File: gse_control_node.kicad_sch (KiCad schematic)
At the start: 9 parts

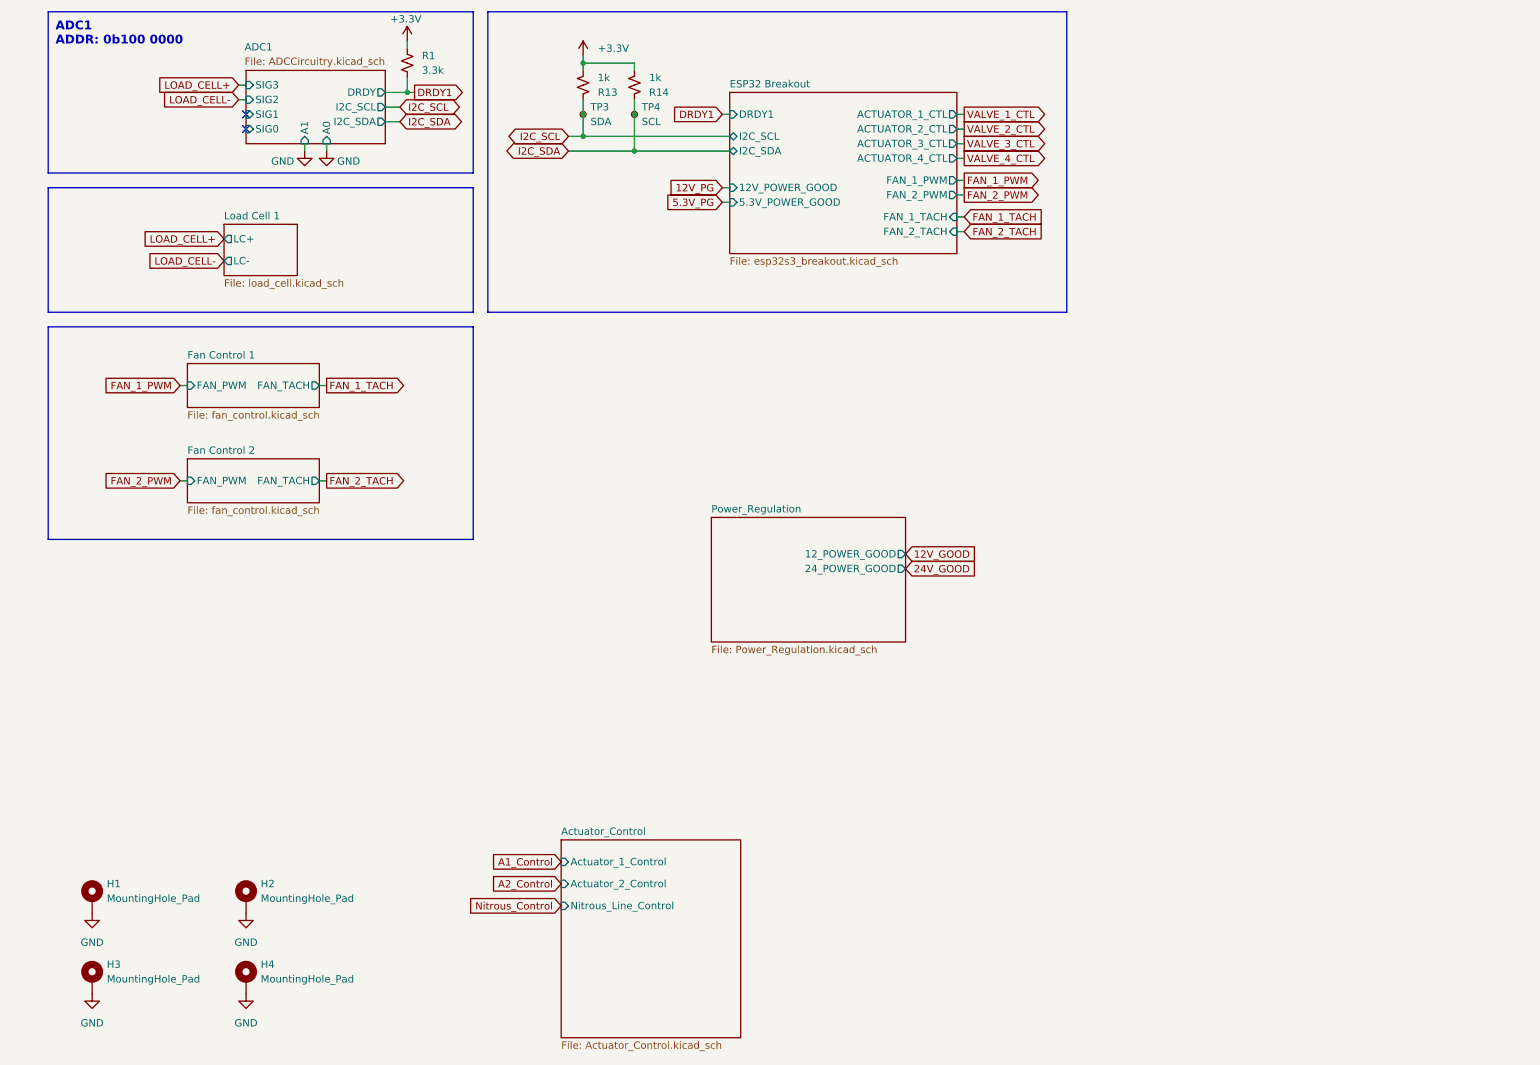
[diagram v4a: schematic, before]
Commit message: update buck converter components and add reverse polarity protection
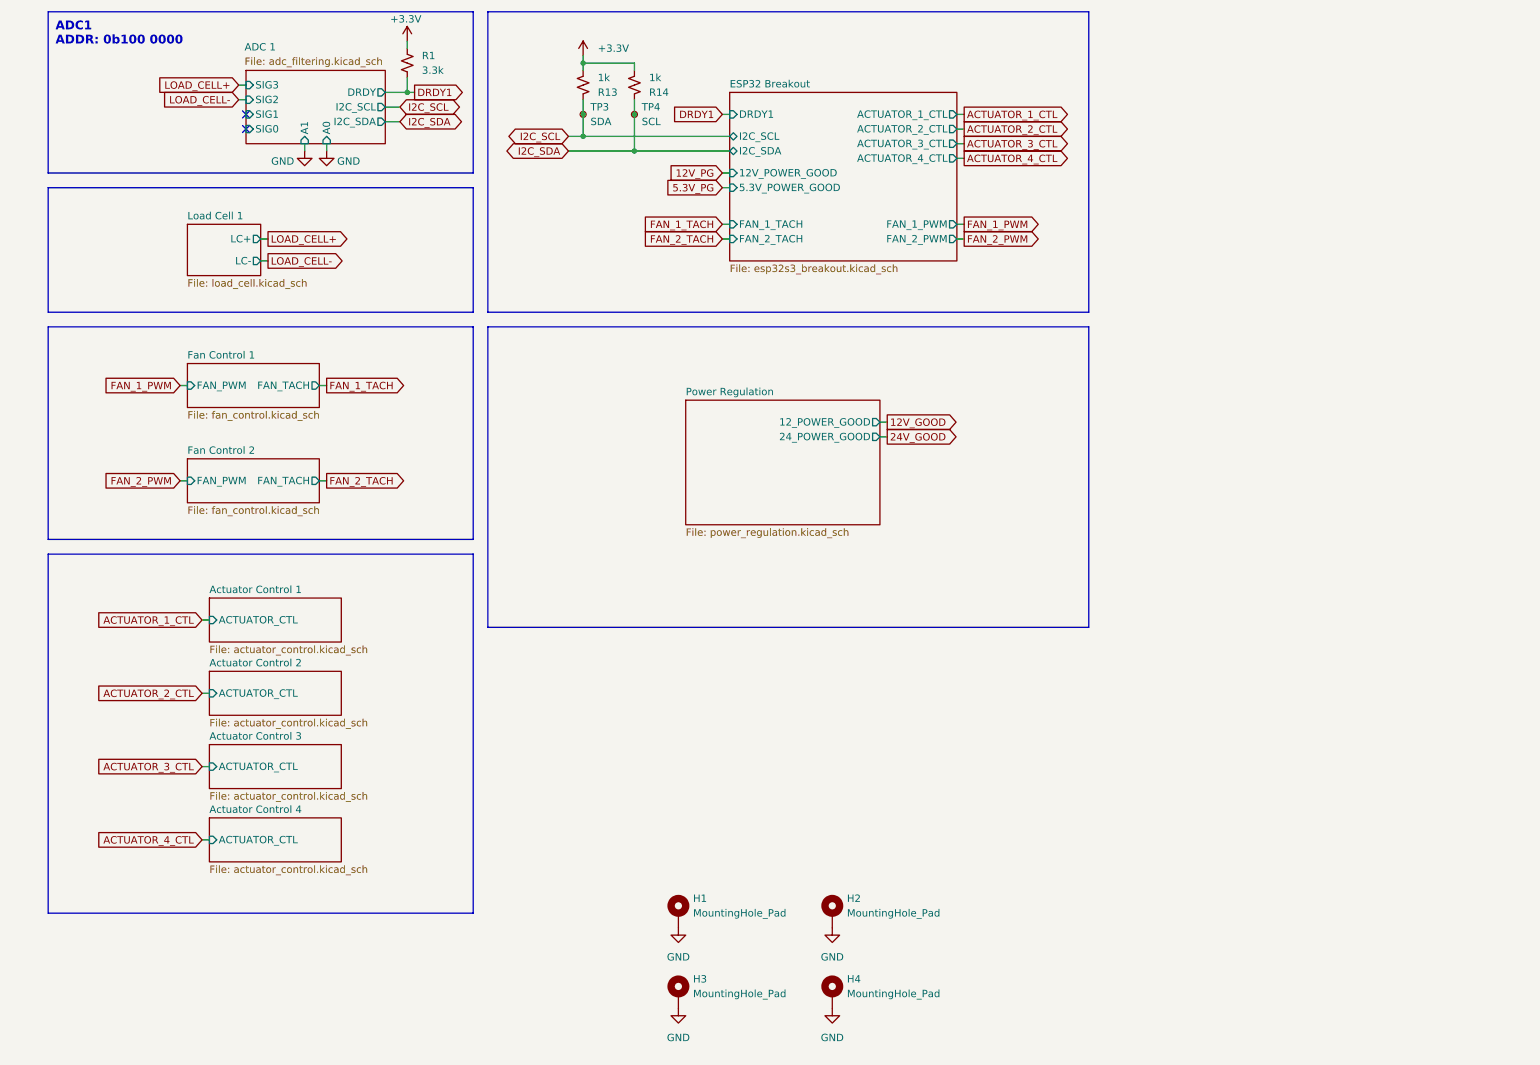
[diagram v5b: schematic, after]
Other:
- sheet ADC1 renamed ADC 1
- sheet Power_Regulation renamed Power Regulation
- removed sheet Actuator_Control
- added sheet Actuator Control 1 (actuator_control.kicad_sch)
- added sheet Actuator Control 2 (actuator_control.kicad_sch)
- added sheet Actuator Control 3 (actuator_control.kicad_sch)
- added sheet Actuator Control 4 (actuator_control.kicad_sch)
- sheet ADC 1: file ADCCircuitry.kicad_sch -> adc_filtering.kicad_sch
- sheet Power Regulation: file Power_Regulation.kicad_sch -> power_regulation.kicad_sch
- moved on the sheet: H1, H2, H3, H4

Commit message: do some pcb routing
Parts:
- added J1: Screw_Terminal_01x02, TerminalBlock_Phoenix:TerminalBlock_Phoenix_MKDS-1,5-2_1x02_P5.00mm_Horizontal, symbol Connector:Screw_Terminal_01x02
- renumbered H3 to H2, H2 to H3, R13 to R2, R14 to R3, TP3 to TP1, TP4 to TP2
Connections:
- net ADC 1/SIG0: now also J1.1 (Pin_1)
- net ADC 1/SIG1: now also J1.2 (Pin_2)
- no-connect marks 2 -> 0
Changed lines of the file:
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@@
 		(color 0 0 0 0)
 	)
-	(no_connect
-		(at 49.53 33.02)
-	)
-	(no_connect
-		(at 49.53 35.56)
-	)
 	(wire
 		(pts
@@
 	(wire
 		(pts
+			(xy 33.02 35.56) (xy 49.53 35.56)
+		)
+		(stroke
+			(width 0)
+			(type default)
+		)
+	)
+	(wire
+		(pts
 			(xy 38.1 96.52) (xy 39.37 96.52)
 		)
@@
 		(pts
 			(xy 73.66 29.21) (xy 77.47 29.21)
+		)
+		(stroke
+			(width 0)
+			(type default)
+		)
+	)
+	(wire
+		(pts
+			(xy 33.02 33.02) (xy 49.53 33.02)
 		)
 		(stroke
@@
 		(in_pos_files yes)
 		(dnp no)
-		(property "Reference" "#PWR07"
+		(property "Reference" "#PWR01"
 			(at 59.69 45.72 0)
 			(hide yes)
@@
 			(project "gse_control_node"
 				(path "/24817451-dfe0-4b9a-9d93-7304529c9d58"
-					(reference "#PWR07")
+					(reference "#PWR01")
 					(unit 1)
 				)
@@
 		(dnp no)
 		(fields_autoplaced yes)
-		(property "Reference" "#PWR03"
+		(property "Reference" "#PWR05"
 			(at 124.46 180.34 0)
 			(hide yes)
@@
 			(project "gse_control_node"
 				(path "/24817451-dfe0-4b9a-9d93-7304529c9d58"
-					(reference "#PWR03")
+					(reference "#PWR05")
 					(unit 1)
 				)
@@
 		(in_pos_files yes)
 		(dnp no)
-		(property "Reference" "#PWR013"
+		(property "Reference" "#PWR03"
 			(at 77.47 24.13 0)
 			(hide yes)
@@
 			(project "gse_control_node"
 				(path "/24817451-dfe0-4b9a-9d93-7304529c9d58"
-					(reference "#PWR013")
+					(reference "#PWR03")
 					(unit 1)
 				)
@@
 		(dnp no)
 		(fields_autoplaced yes)
-		(property "Reference" "#PWR06"
+		(property "Reference" "#PWR08"
 			(at 151.13 194.31 0)
 			(hide yes)
@@
 			(project "gse_control_node"
 				(path "/24817451-dfe0-4b9a-9d93-7304529c9d58"
-					(reference "#PWR06")
+					(reference "#PWR08")
 					(unit 1)
 				)
@@
 		(dnp no)
 		(fields_autoplaced yes)
-		(property "Reference" "R13"
+		(property "Reference" "R2"
 			(at 110.49 29.2101 0)
 			(show_name no)
@@
 			(project "gse_control_node"
 				(path "/24817451-dfe0-4b9a-9d93-7304529c9d58"
-					(reference "R13")
+					(reference "R2")
 					(unit 1)
 				)
@@
 		(in_pos_files yes)
 		(dnp no)
-		(property "Reference" "#PWR09"
+		(property "Reference" "#PWR02"
 			(at 63.5 45.72 0)
 			(hide yes)
@@
 			(project "gse_control_node"
 				(path "/24817451-dfe0-4b9a-9d93-7304529c9d58"
-					(reference "#PWR09")
+					(reference "#PWR02")
 					(unit 1)
 				)
@@
 		(dnp no)
 		(fields_autoplaced yes)
-		(property "Reference" "R14"
+		(property "Reference" "R3"
 			(at 119.38 29.2101 0)
 			(show_name no)
@@
 			(project "gse_control_node"
 				(path "/24817451-dfe0-4b9a-9d93-7304529c9d58"
-					(reference "R14")
+					(reference "R3")
 					(unit 1)
 				)
@@
 		(dnp no)
 		(fields_autoplaced yes)
-		(property "Reference" "#PWR020"
+		(property "Reference" "#PWR04"
 			(at 107.95 26.67 0)
 			(hide yes)
@@
 			(project "gse_control_node"
 				(path "/24817451-dfe0-4b9a-9d93-7304529c9d58"
-					(reference "#PWR020")
+					(reference "#PWR04")
 					(unit 1)
 				)
@@
 		(dnp no)
 		(fields_autoplaced yes)
-		(property "Reference" "#PWR05"
+		(property "Reference" "#PWR06"
 			(at 124.46 194.31 0)
 			(hide yes)
@@
 			(project "gse_control_node"
 				(path "/24817451-dfe0-4b9a-9d93-7304529c9d58"
-					(reference "#PWR05")
+					(reference "#PWR06")
 					(unit 1)
 				)
@@
 		(dnp no)
 		(fields_autoplaced yes)
-		(property "Reference" "#PWR04"
+		(property "Reference" "#PWR07"
 			(at 151.13 180.34 0)
 			(hide yes)
@@
 			(project "gse_control_node"
 				(path "/24817451-dfe0-4b9a-9d93-7304529c9d58"
-					(reference "#PWR04")
+					(reference "#PWR07")
+					(unit 1)
+				)
+			)
+		)
+	)
+	(symbol
+		(lib_id "Connector:Screw_Terminal_01x02")
+		(at 27.94 35.56 180)
+		(unit 1)
+		(body_style 1)
+		(exclude_from_sim no)
+		(in_bom yes)
+		(on_board yes)
+		(in_pos_files yes)
+		(dnp no)
+		(property "Reference" "J1"
+			(at 27.94 30.226 0)
+			(show_name no)
+			(do_not_autoplace no)
+			(effects
+				(font
+					(size 1.27 1.27)
+				)
+			)
+		)
+		(property "Value" "Screw_Terminal_01x02"
+			(at 27.94 29.21 0)
+			(hide yes)
+			(show_name no)
+			(do_not_autoplace no)
+			(effects
+				(font
+					(size 1.27 1.27)
+				)
+			)
+		)
+		(property "Footprint" "TerminalBlock_Phoenix:TerminalBlock_Phoenix_MKDS-1,5-2_1x02_P5.00mm_Horizontal"
+			(at 27.94 35.56 0)
+			(hide yes)
+			(show_name no)
+			(do_not_autoplace no)
+			(effects
+				(font
+					(size 1.27 1.27)
+				)
+			)
+		)
+		(property "Datasheet" ""
+			(at 27.94 35.56 0)
+			(hide yes)
+			(show_name no)
+			(do_not_autoplace no)
+			(effects
+				(font
+					(size 1.27 1.27)
+				)
+			)
+		)
+		(property "Description" "Generic screw terminal, single row, 01x02, script generated (kicad-library-utils/schlib/autogen/connector/)"
+			(at 27.94 35.56 0)
+			(hide yes)
+			(show_name no)
+			(do_not_autoplace no)
+			(effects
+				(font
+					(size 1.27 1.27)
+				)
+			)
+		)
+		(pin "1"
+		)
+		(pin "2"
+		)
+		(instances
+			(project "gse_control_node"
+				(path "/24817451-dfe0-4b9a-9d93-7304529c9d58"
+					(reference "J1")
 					(unit 1)
 				)
@@
 		(dnp no)
 		(fields_autoplaced yes)
-		(property "Reference" "TP3"
+		(property "Reference" "TP1"
 			(at 109.22 31.7499 0)
 			(show_name no)
@@
 			(project "gse_control_node"
 				(path "/24817451-dfe0-4b9a-9d93-7304529c9d58"
-					(reference "TP3")
+					(reference "TP1")
 					(unit 1)
 				)
@@
 		(dnp no)
 		(fields_autoplaced yes)
-		(property "Reference" "H2"
+		(property "Reference" "H3"
 			(at 153.67 168.9099 0)
 			(show_name no)
@@
 			(project "gse_control_node"
 				(path "/24817451-dfe0-4b9a-9d93-7304529c9d58"
-					(reference "H2")
+					(reference "H3")
 					(unit 1)
 				)
@@
 		(dnp no)
 		(fields_autoplaced yes)
-		(property "Reference" "TP4"
+		(property "Reference" "TP2"
 			(at 118.11 31.7499 0)
 			(show_name no)
@@
 			(project "gse_control_node"
 				(path "/24817451-dfe0-4b9a-9d93-7304529c9d58"
-					(reference "TP4")
+					(reference "TP2")
 					(unit 1)
 				)
@@
 		(dnp no)
 		(fields_autoplaced yes)
-		(property "Reference" "H3"
+		(property "Reference" "H2"
 			(at 127 182.8799 0)
 			(show_name no)
@@
 			(project "gse_control_node"
 				(path "/24817451-dfe0-4b9a-9d93-7304529c9d58"
-					(reference "H3")
+					(reference "H2")
 					(unit 1)
 				)

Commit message: finish pcb routing
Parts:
- removed TP1: SDA, TestPoint:TestPoint_Pad_D1.5mm, symbol Connector:TestPoint_Small
- removed TP2: SCL, TestPoint:TestPoint_Pad_D1.5mm, symbol Connector:TestPoint_Small
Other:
- sheet ESP32 Breakout ports: added 5.17V_POWER_GOOD; removed 5.3V_POWER_GOOD
- sheet Power Regulation ports: added 5.17_POWER_GOOD; removed 24_POWER_GOOD

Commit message: remove unneccesary component fields
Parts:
- H1, H2, H3, H4: LCSC (none) -> N/A
- J1: LCSC (none) -> N/A; now left out of the parts list
- R1: value 3.3k -> 3.3kΩ; LCSC C25890 -> (none); MPN 0402WGF3301TCE -> (none)
- R2, R3: value 1k -> 1kΩ; LCSC C11702 -> (none)
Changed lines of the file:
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@@
 		(in_bom no)
 		(on_board yes)
-		(in_pos_files yes)
+		(in_pos_files no)
 		(dnp no)
 		(fields_autoplaced yes)
@@
 			)
 		)
+		(property "LCSC" "N/A"
+			(at 151.13 185.42 0)
+			(hide yes)
+			(show_name no)
+			(do_not_autoplace no)
+			(effects
+				(font
+					(size 1.27 1.27)
+				)
+			)
+		)
 		(pin "1"
 		)
@@
 		(in_bom no)
 		(on_board yes)
-		(in_pos_files yes)
+		(in_pos_files no)
 		(dnp no)
 		(fields_autoplaced yes)
@@
 			)
 		)
+		(property "LCSC" "N/A"
+			(at 124.46 171.45 0)
+			(hide yes)
+			(show_name no)
+			(do_not_autoplace no)
+			(effects
+				(font
+					(size 1.27 1.27)
+				)
+			)
+		)
 		(pin "1"
 		)
@@
 			)
 		)
-		(property "Value" "1k"
+		(property "Value" "1kΩ"
 			(at 110.49 26.6701 0)
 			(show_name no)
@@
 			)
 		)
-		(property "ADC Number" ""
-			(at 107.95 27.94 0)
-			(hide yes)
-			(show_name no)
-			(do_not_autoplace no)
-			(effects
-				(font
-					(size 1.27 1.27)
-				)
-			)
-		)
-		(property "DCR" ""
-			(at 107.95 27.94 0)
-			(hide yes)
-			(show_name no)
-			(do_not_autoplace no)
-			(effects
-				(font
-					(size 1.27 1.27)
-				)
-			)
-		)
-		(property "I2C Address" ""
-			(at 107.95 27.94 0)
-			(hide yes)
-			(show_name no)
-			(do_not_autoplace no)
-			(effects
-				(font
-					(size 1.27 1.27)
-				)
-			)
-		)
-		(property "Irated" ""
-			(at 107.95 27.94 0)
-			(hide yes)
-			(show_name no)
-			(do_not_autoplace no)
-			(effects
-				(font
-					(size 1.27 1.27)
-				)
-			)
-		)
-		(property "Isat" ""
-			(at 107.95 27.94 0)
-			(hide yes)
-			(show_name no)
-			(do_not_autoplace no)
-			(effects
-				(font
-					(size 1.27 1.27)
-				)
-			)
-		)
-		(property "MFG" ""
-			(at 107.95 27.94 0)
-			(hide yes)
-			(show_name no)
-			(do_not_autoplace no)
-			(effects
-				(font
-					(size 1.27 1.27)
-				)
-			)
-		)
-		(property "MFR" ""
-			(at 107.95 27.94 0)
-			(hide yes)
-			(show_name no)
-			(do_not_autoplace no)
-			(effects
-				(font
-					(size 1.27 1.27)
-				)
-			)
-		)
-		(property "LCSC" "C11702"
+		(property "LCSC" ""
 			(at 107.95 27.94 0)
 			(hide yes)
@@
 			)
 		)
-		(property "Value" "3.3k"
+		(property "Value" "3.3kΩ"
 			(at 80.01 25.3999 0)
 			(show_name no)
@@
 			)
 		)
-		(property "MPN" "0402WGF3301TCE"
-			(at 77.47 24.13 0)
-			(hide yes)
-			(show_name no)
-			(do_not_autoplace no)
-			(effects
-				(font
-					(size 1.27 1.27)
-				)
-			)
-		)
-		(property "LCSC" "C25890"
-			(at 77.47 24.13 0)
-			(hide yes)
-			(show_name no)
-			(do_not_autoplace no)
-			(effects
-				(font
-					(size 1.27 1.27)
-				)
-			)
-		)
-		(property "ADC Number" ""
-			(at 77.47 24.13 0)
-			(hide yes)
-			(show_name no)
-			(do_not_autoplace no)
-			(effects
-				(font
-					(size 1.27 1.27)
-				)
-			)
-		)
-		(property "DCR" ""
-			(at 77.47 24.13 0)
-			(hide yes)
-			(show_name no)
-			(do_not_autoplace no)
-			(effects
-				(font
-					(size 1.27 1.27)
-				)
-			)
-		)
-		(property "I2C Address" ""
-			(at 77.47 24.13 0)
-			(hide yes)
-			(show_name no)
-			(do_not_autoplace no)
-			(effects
-				(font
-					(size 1.27 1.27)
-				)
-			)
-		)
-		(property "Irated" ""
-			(at 77.47 24.13 0)
-			(hide yes)
-			(show_name no)
-			(do_not_autoplace no)
-			(effects
-				(font
-					(size 1.27 1.27)
-				)
-			)
-		)
-		(property "Isat" ""
-			(at 77.47 24.13 0)
-			(hide yes)
-			(show_name no)
-			(do_not_autoplace no)
-			(effects
-				(font
-					(size 1.27 1.27)
-				)
-			)
-		)
-		(property "MFG" ""
-			(at 77.47 24.13 0)
-			(hide yes)
-			(show_name no)
-			(do_not_autoplace no)
-			(effects
-				(font
-					(size 1.27 1.27)
-				)
-			)
-		)
-		(property "MFR" ""
+		(property "LCSC" ""
 			(at 77.47 24.13 0)
 			(hide yes)
@@
 			)
 		)
-		(property "Value" "1k"
+		(property "Value" "1kΩ"
 			(at 119.38 26.6701 0)
 			(show_name no)
@@
 			)
 		)
-		(property "ADC Number" ""
-			(at 116.84 27.94 0)
-			(hide yes)
-			(show_name no)
-			(do_not_autoplace no)
-			(effects
-				(font
-					(size 1.27 1.27)
-				)
-			)
-		)
-		(property "DCR" ""
-			(at 116.84 27.94 0)
-			(hide yes)
-			(show_name no)
-			(do_not_autoplace no)
-			(effects
-				(font
-					(size 1.27 1.27)
-				)
-			)
-		)
-		(property "I2C Address" ""
-			(at 116.84 27.94 0)
-			(hide yes)
-			(show_name no)
-			(do_not_autoplace no)
-			(effects
-				(font
-					(size 1.27 1.27)
-				)
-			)
-		)
-		(property "Irated" ""
-			(at 116.84 27.94 0)
-			(hide yes)
-			(show_name no)
-			(do_not_autoplace no)
-			(effects
-				(font
-					(size 1.27 1.27)
-				)
-			)
-		)
-		(property "Isat" ""
-			(at 116.84 27.94 0)
-			(hide yes)
-			(show_name no)
-			(do_not_autoplace no)
-			(effects
-				(font
-					(size 1.27 1.27)
-				)
-			)
-		)
-		(property "MFG" ""
-			(at 116.84 27.94 0)
-			(hide yes)
-			(show_name no)
-			(do_not_autoplace no)
-			(effects
-				(font
-					(size 1.27 1.27)
-				)
-			)
-		)
-		(property "MFR" ""
-			(at 116.84 27.94 0)
-			(hide yes)
-			(show_name no)
-			(do_not_autoplace no)
-			(effects
-				(font
-					(size 1.27 1.27)
-				)
-			)
-		)
-		(property "LCSC" "C11702"
+		(property "LCSC" ""
 			(at 116.84 27.94 0)
 			(hide yes)
@@
 		(body_style 1)
 		(exclude_from_sim no)
-		(in_bom yes)
-		(on_board yes)
-		(in_pos_files yes)
+		(in_bom no)
+		(on_board yes)
+		(in_pos_files no)
 		(dnp no)
 		(property "Reference" "J1"
@@
 			)
 		)
+		(property "LCSC" "N/A"
+			(at 27.94 35.56 0)
+			(hide yes)
+			(show_name no)
+			(do_not_autoplace no)
+			(effects
+				(font
+					(size 1.27 1.27)
+				)
+			)
+		)
 		(pin "1"
 		)
@@
 		(in_bom no)
 		(on_board yes)
-		(in_pos_files yes)
+		(in_pos_files no)
 		(dnp no)
 		(fields_autoplaced yes)
@@
 			)
 		)
+		(property "LCSC" "N/A"
+			(at 151.13 171.45 0)
+			(hide yes)
+			(show_name no)
+			(do_not_autoplace no)
+			(effects
+				(font
+					(size 1.27 1.27)
+				)
+			)
+		)
 		(pin "1"
 		)
@@
 		(in_bom no)
 		(on_board yes)
-		(in_pos_files yes)
+		(in_pos_files no)
 		(dnp no)
 		(fields_autoplaced yes)
@@
 			(at 124.46 185.42 0)
 			(hide yes)
+			(show_name no)
+			(do_not_autoplace no)
+			(effects
+				(font
+					(size 1.27 1.27)
+				)
+			)
+		)
+		(property "LCSC" "N/A"
+			(at 124.46 185.42 0)
+			(hide yes)
